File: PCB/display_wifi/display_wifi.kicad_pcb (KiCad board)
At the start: 2 copper layers, 50 x 50 mm, 17 parts, among them J1 Conn_01x02, J2 Conn_01x10, SW1 SW_Push, SW2 SW_Push, SW3 SW_Push, U1 NINA-W132, U2 OPT4001DNPRQ1

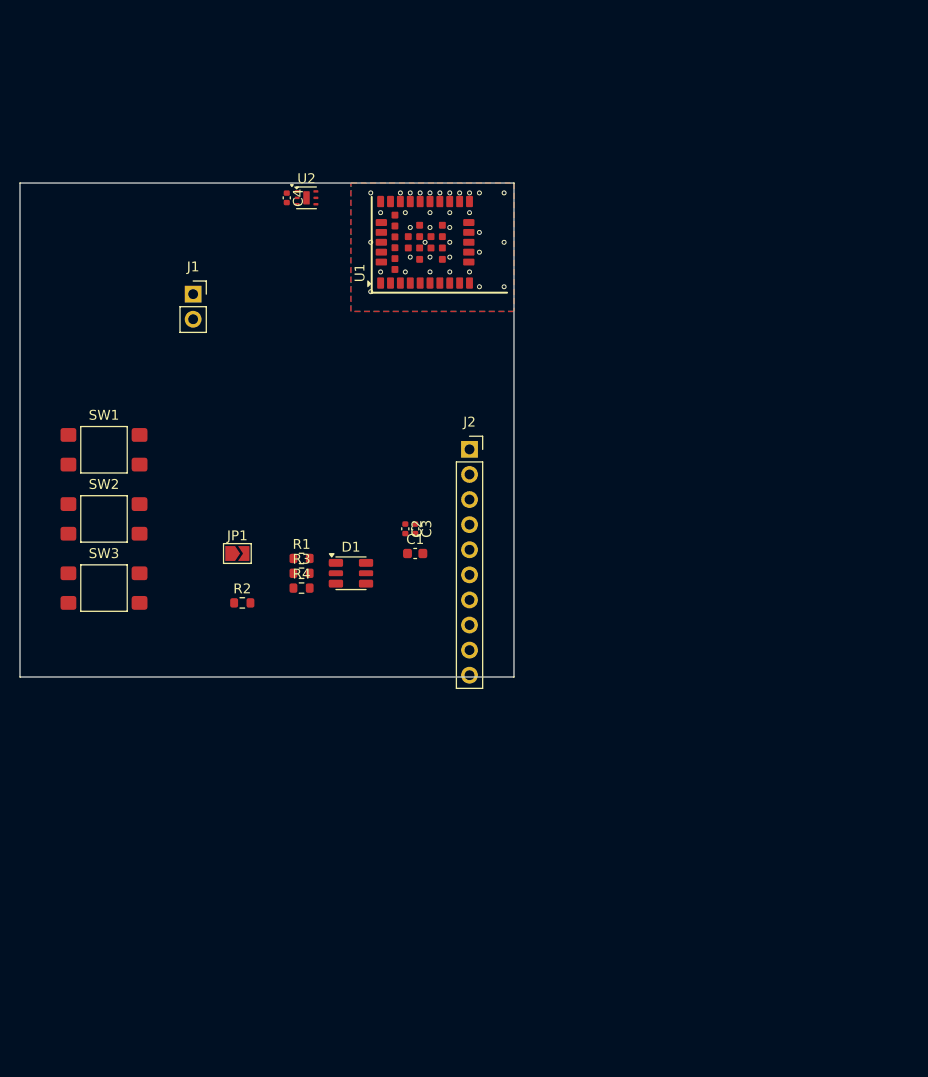
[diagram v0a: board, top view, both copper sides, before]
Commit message: Added light sensor, IR remote sensor, test connectors, and routed PCB for display
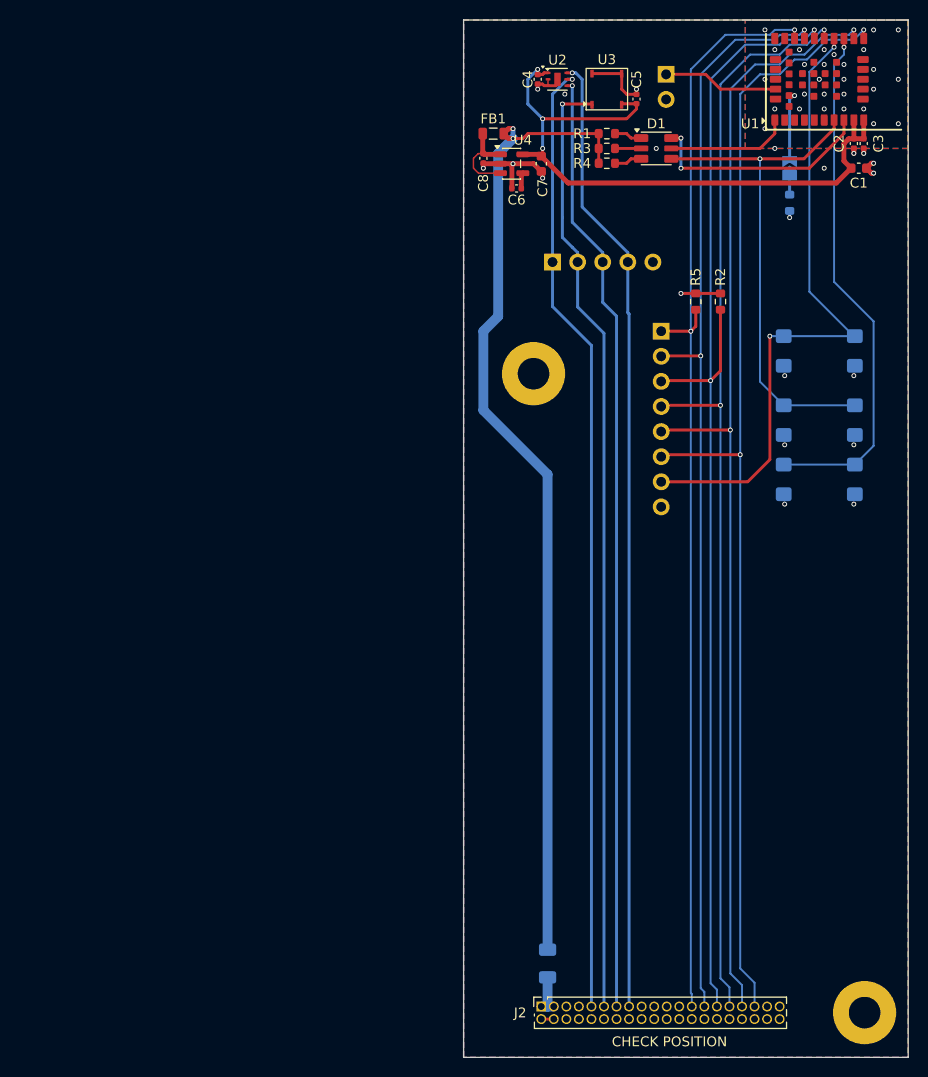
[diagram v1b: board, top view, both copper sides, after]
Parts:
- added C5: 0.1u, Capacitor_SMD:C_0402_1005Metric, F.Cu at (162.4, 41.5)
- added C6: 470p, Capacitor_SMD:C_0402_1005Metric, F.Cu at (150.3, 50.5)
- added C7: 4.7u, Capacitor_SMD:C_0603_1608Metric, F.Cu at (152.8, 48.0)
- added C8: 1u, Capacitor_SMD:C_0402_1005Metric, F.Cu at (146.9, 47.5)
- added F1: 500mA, Fuse:Fuse_1206_3216Metric, B.Cu at (153.4, 129.0)
- added FB1: 600R, Inductor_SMD:L_0805_2012Metric, F.Cu at (147.9, 45.0)
- added H1: M3, MountingHole:MountingHole_3.2mm_M3_Pad, F.Cu at (152.0, 69.3)
- added H2: M3, MountingHole:MountingHole_3.2mm_M3_Pad, F.Cu at (185.5, 134.0)
- added J3: Conn_01x08, Connector_PinHeader_2.54mm:PinHeader_1x08_P2.54mm_Vertical, B.Cu at (164.9, 65.0)
- added J4: Conn_01x05, Connector_PinHeader_2.54mm:PinHeader_1x05_P2.54mm_Vertical, B.Cu at (153.9, 58.0)
- added R5: 10k, Resistor_SMD:R_0603_1608Metric, F.Cu at (168.4, 62.0)
- added R7: 620R, Resistor_SMD:R_0603_1608Metric, B.Cu at (177.9, 52.0)
- added U3: TSOP37436TT, DWlib:Vishay_BELOBOG-4Pin, F.Cu at (159.4, 40.5)
- added U4: MIC5219-3.3YM5, Package_TO_SOT_SMD:SOT-23-5, F.Cu at (149.8, 48.0)
- J1: footprint Connector_PinSocket_2.54mm:PinSocket_1x02_P2.54mm_Vertical -> Connector_PinHeader_2.54mm:PinHeader_1x02_P2.54mm_Vertical; moved to B.Cu
- J2: value Conn_01x10 -> 1.27 mm pitch; footprint Connector_PinSocket_2.54mm:PinSocket_1x10_P2.54mm_Vertical -> Connector_PinSocket_1.27mm:PinSocket_2x20_P1.27mm_Vertical
- JP1: moved to B.Cu
- R2: value 10K -> 10k
- SW1, SW2, SW3: value SW_Push -> TL3305; moved to B.Cu
- moved SW3 74.4 mm to (180.9, 74.0), turned to 180 degrees
- moved SW1 73.1 mm to (180.9, 67.0)
- moved SW2 72.5 mm to (180.9, 80.0)
- moved JP1 68.2 mm to (177.9, 48.5), turned to 90 degrees
- moved C2 59.9 mm to (184.4, 46.0)
- moved C3 59.9 mm to (185.4, 46.0)
- moved C1 59.5 mm to (184.9, 48.5)
- moved R2 57.2 mm to (170.9, 62.0), turned to 90 degrees
- moved J2 56.9 mm to (152.8, 133.4), turned to 90 degrees
- moved D1 53.0 mm to (164.4, 46.5)
- moved R1 53.0 mm to (159.4, 45.0)
- moved R3 53.0 mm to (159.4, 46.5)
- moved R4 53.0 mm to (159.4, 48.0)
- moved J1 52.8 mm to (165.4, 39.0), turned to 180 degrees
- moved U1 43.2 mm to (186.2, 39.5)
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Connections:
- J2 pad 1: unconnected-(J2-Pin_1-Pad1) -> +5VIN
- J2 pad 2: unconnected-(J2-Pin_2-Pad2) -> +3.3VIN
- J2 pad 3: unconnected-(J2-Pin_3-Pad3) -> +5VIN
- J2 pad 4: unconnected-(J2-Pin_4-Pad4) -> +3.3VIN
- J2 pad 6: unconnected-(J2-Pin_6-Pad6) -> GND
- J2 pad 7: unconnected-(J2-Pin_7-Pad7) -> GND
- J2 pad 9: unconnected-(J2-Pin_9-Pad9) -> /ALS_INT
- JP1 pad 1: unconnected-(JP1-A-Pad1) -> Net-(JP1-A)
- R2 pad 1: unconnected-(R2-Pad1) -> UART_CTS
- R2 pad 2: unconnected-(R2-Pad2) -> GND
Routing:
- net UART_CTS: track 0.00 -> 120.2 mm, vias 1 -> 2
- net UART_DTR: track 0.00 -> 117.1 mm, vias 1 -> 2
- net UART_DSR: track 0.00 -> 116.3 mm, vias 1 -> 2
- net UART_RTS: track 0.00 -> 113.4 mm, vias 1 -> 2
- net UART_RXD: track 0.00 -> 113.3 mm, vias 1 -> 2
- net UART_TXD: track 0.00 -> 111.8 mm, vias 1 -> 2
- net +5V: track 0.00 -> 101.2 mm, vias 0 -> 2
- net /SDA: track 0.00 -> 97.6 mm, vias 0 -> 1
- net /ALS_INT: track 0.00 -> 97.2 mm, vias 0 -> 1
- net /IR_IN: track 0.00 -> 96.1 mm, vias 0 -> 1
- net /SCL: track 0.00 -> 95.6 mm, vias 0 -> 1
- net +3.3V: track 0.00 -> 67.3 mm, vias 0 -> 3
- net /RSTN: track 0.00 -> 66.2 mm, vias 1 -> 2
- net /SW2: track 0.00 -> 53.2 mm
- net /SW1_GRN: track 0.00 -> 51.8 mm, vias 0 -> 1
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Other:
- board size 50 x 50 mm -> 45 x 105 mm
- board text added: "CHECK POSITION"
- board text added: "CTS-I"
- board text added: "DSR-I"
- board text added: "DTR-O"
- board text added: "GND"
- board text added: "INT"
- board text added: "IR"
- board text added: "RESET"
- board text added: "RSTN"
- board text added: "RTS-O"
- board text added: "RXD-I"
- board text added: "SCL"
- board text added: "SDA"
- board text added: "SWITCH 1"
- board text added: "SWITCH 2"
- board text added: "TXD-O"

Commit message: Added passthrough for power and SWD to simplify connections. Added part numbers.
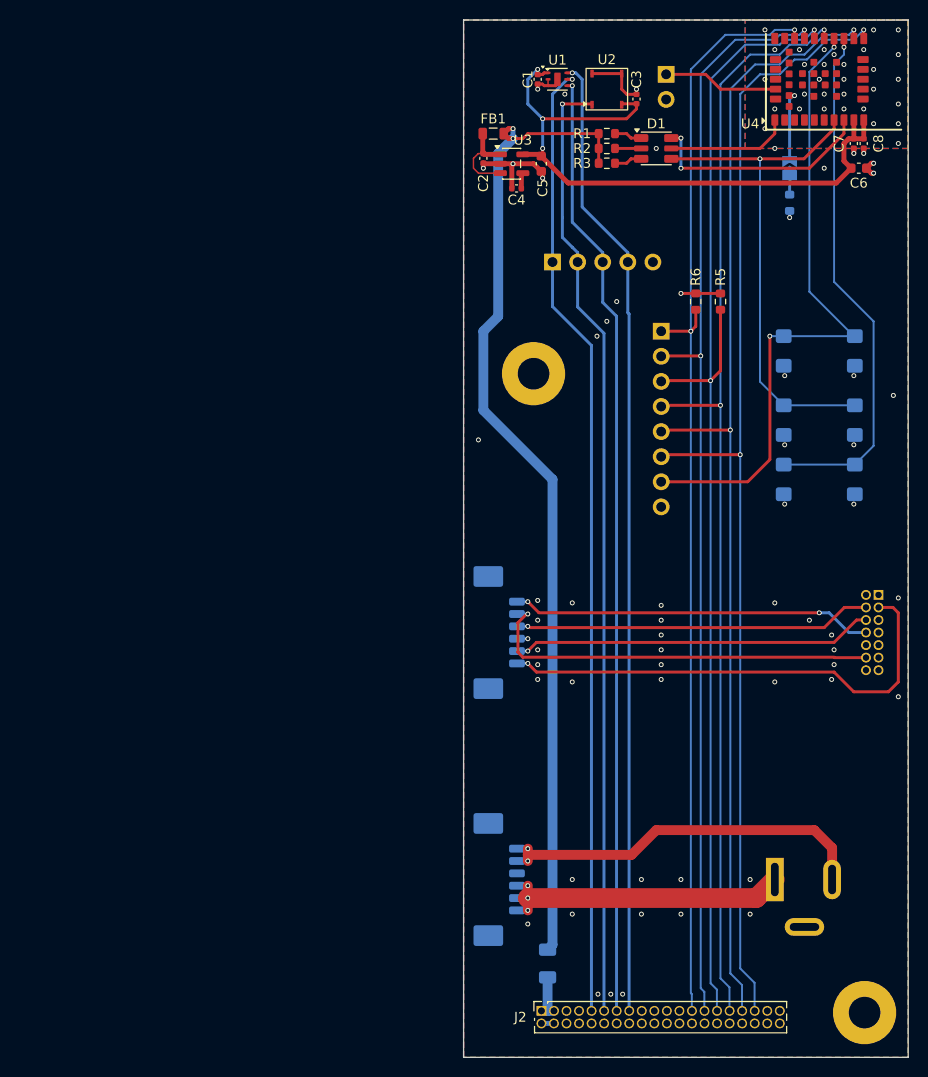
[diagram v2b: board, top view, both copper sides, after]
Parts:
- added J5: 694106301002, Connector_BarrelJack:BarrelJack_Wuerth_6941xx301002, B.Cu at (176.4, 120.5)
- added J6: Conn_ST_STDC14, Connector_PinHeader_1.27mm:PinHeader_2x07_P1.27mm_Vertical, B.Cu at (186.9, 91.7)
- added J7: 53261-0671, Connector_Molex:Molex_PicoBlade_53261-0671_1x06-1MP_P1.25mm_Horizontal, B.Cu at (147.9, 120.5)
- added J8: 53261-0671, Connector_Molex:Molex_PicoBlade_53261-0671_1x06-1MP_P1.25mm_Horizontal, B.Cu at (147.9, 95.5)
- U2: renamed from U3; value TSOP37436TT -> TSOP37438
- moved J2 0.44 mm to (152.8, 133.8)
- renumbered C4 to C1, C8 to C2, C5 to C3, C6 to C4, C7 to C5, C1 to C6, C2 to C7, C3 to C8, R3 to R2, R4 to R3, R7 to R4, R2 to R5, R5 to R6, U2 to U1, U4 to U3, U1 to U4
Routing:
- net /Passthrough/SWD_VCC: track 0.00 -> 49.4 mm, vias 0 -> 1
- net /Passthrough/SWD_RSTN: track 0.00 -> 40.9 mm, vias 0 -> 1
- net GND: track 28.2 -> 68.6 mm, vias 49 -> 94
- net /Passthrough/SWCLK: track 0.00 -> 36.6 mm, vias 0 -> 1
- net /Passthrough/SWO: track 0.00 -> 36.6 mm, vias 0 -> 2
- net /Passthrough/SWDIO: track 0.00 -> 36.2 mm, vias 0 -> 1
- net /Passthrough/+12V_IN: track 0.00 -> 31.6 mm, vias 0 -> 3
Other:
- board text added: "+12V"
- board text added: "PWR"
- board text added: "SWD"
- board text added: "Weather Station Wi-Fi Interface"
- board text added: "v1.00 Nov 2025"
- board text removed: "CHECK POSITION"

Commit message: Updated PCB to v1.1
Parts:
- added C9: 22u, Capacitor_SMD:C_1210_3225Metric, F.Cu at (181.4, 52.0)
- added R7: 1.2k, Resistor_SMD:R_0603_1608Metric, F.Cu at (161.4, 55.0)
- added R8: 1.2k, Resistor_SMD:R_0603_1608Metric, F.Cu at (158.9, 55.0)
- added R9: 10k, Resistor_SMD:R_0603_1608Metric, F.Cu at (153.9, 55.0)
- R1, R3: value 360R -> 1.8k
- R2: value 620R -> 3.3k
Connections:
- J2 pad 23: unconnected-(J2-Pin_23-Pad23) -> DEBUG_TXD
- J2 pad 33: UART_DSR -> unconnected-(J2-Pin_33-Pad33)
- J2 pad 35: UART_DTR -> UART_DSR
- J2 pad 36: unconnected-(J2-Pin_36-Pad36) -> UART_DTR
- J6 pad 14: unconnected-(J6-VCP_TX-Pad14) -> DEBUG_TXD
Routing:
- net DEBUG_TXD: track 0.00 -> 50.7 mm, vias 0 -> 1
- net +3.3V: track 67.3 -> 81.0 mm
- net UART_DTR: track 117.6 -> 128.0 mm
- net GND: track 68.6 -> 72.3 mm, vias 94 -> 97
- net /SDA: track 98.1 -> 100.3 mm
- net /SCL: track 96.1 -> 98.3 mm
- net /ALS_INT: track 97.6 -> 99.8 mm
- net UART_DSR: track 116.7 -> 117.2 mm
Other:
- outline, holes or cut-outs redrawn
- board text added: "Merry Christmas 2025 Dad!"
- board text added: "v1.10 Nov 2025"
- board text removed: "v1.00 Nov 2025"
